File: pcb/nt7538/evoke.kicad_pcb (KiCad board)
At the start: 2 copper layers, 60 x 45 mm, 41 parts, among them J1 Conn_01x03_Male, J2 BACKLIGHT_CONN, Q1 Q_NMOS_GSD, U1 STM32F103C8Tx

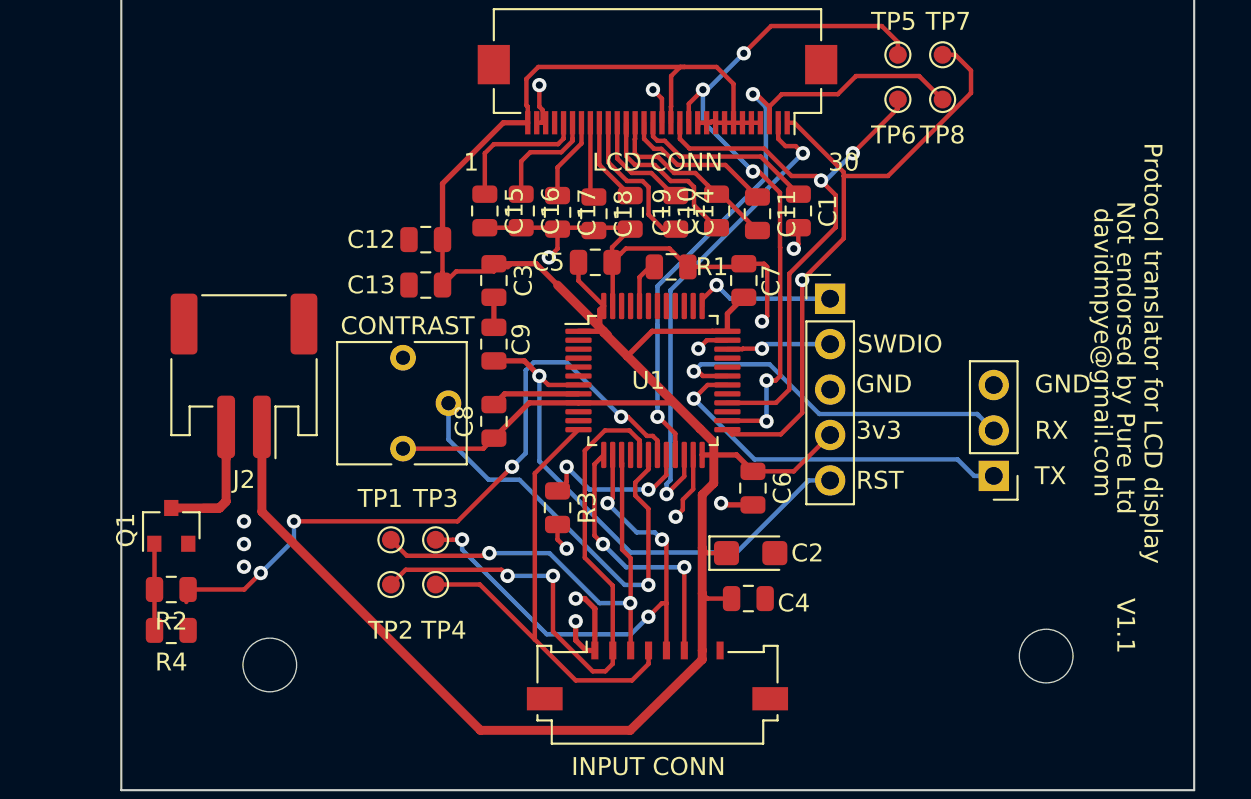
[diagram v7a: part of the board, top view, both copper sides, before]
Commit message: Updates to v1.2 for NT pcb - hole spacing redone
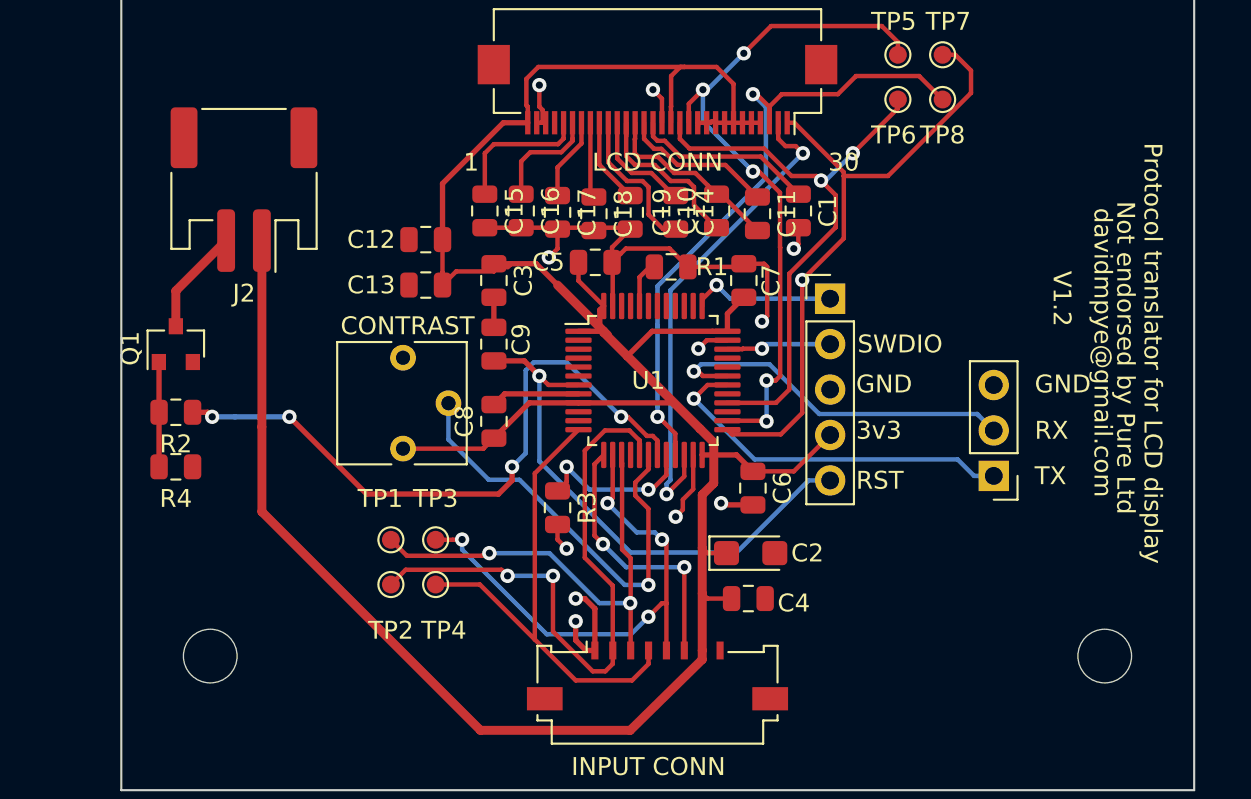
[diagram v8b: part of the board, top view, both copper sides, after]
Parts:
- moved J2 10.4 mm to (81.8, 42.9)
- moved Q1 10.2 mm to (78.0, 51.6)
- moved R2 9.91 mm to (78.0, 55.4)
- moved R4 9.15 mm to (78.0, 58.4)
- moved REF** 3.36 mm to (79.9, 69.0)
- moved REF** 3.27 mm to (129.9, 69.0)
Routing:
- net +3V3: track 151.0 -> 161.4 mm
- net Net-(J2-Pad2): track 8.83 -> 5.95 mm
- net LCD_BACKLIGHT_PWM: track 38.4 -> 36.7 mm
- net Net-(Q1-Pad1): track 4.85 -> 5.86 mm
- net GND: vias 14 -> 11
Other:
- board text added: "V1.2"
- board text removed: "V1.1"
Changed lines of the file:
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@@
     (thickness 1.6)
     (drawings 17)
-    (tracks 467)
+    (tracks 460)
     (zones 0)
     (modules 41)
@@
   )
   (setup
-    (last_trace_width 0.25)
+    (last_trace_width 0.3)
     (user_trace_width 0.3)
     (user_trace_width 0.5)
@@
   )
   (module MountingHole:MountingHole_3mm locked (layer F.Cu)
-    (at 126.63 69)
+    (at 129.902 69)
     (descr "Mounting Hole 3mm, no annular")
     (tags "mounting hole 3mm no annular")
@@
   )
   (module MountingHole:MountingHole_3mm locked (layer F.Cu)
-    (at 83.23 69.496)
+    (at 79.902 69)
     (descr "Mounting Hole 3mm, no annular")
     (tags "mounting hole 3mm no annular")
@@
   )
   (module Package_TO_SOT_SMD:SOT-23 (layer F.Cu)
-    (at 77.724 61.722 90)
+    (at 77.978 51.562 90)
     (descr "SOT-23, Standard")
     (tags SOT-23)
@@
   )
   (module Resistor_SMD:R_0805_2012Metric (layer F.Cu)
-    (at 77.724 65.278)
+    (at 77.978 55.372)
     (descr "Resistor SMD 0805 (2012 Metric), square (rectangular) end terminal, IPC_7351 nominal, (Body size source: https://docs.google.com/spreadsheets/d/1BsfQQcO9C6DZCsRaXUlFlo91Tg2WpOkGARC1WS5S8t0/edit?usp=sharing), generated with kicad-footprint-generator")
     (tags resistor)
@@
   )
   (module Resistor_SMD:R_0805_2012Metric (layer F.Cu)
-    (at 77.724 67.564)
+    (at 77.978 58.42)
     (descr "Resistor SMD 0805 (2012 Metric), square (rectangular) end terminal, IPC_7351 nominal, (Body size source: https://docs.google.com/spreadsheets/d/1BsfQQcO9C6DZCsRaXUlFlo91Tg2WpOkGARC1WS5S8t0/edit?usp=sharing), generated with kicad-footprint-generator")
     (tags resistor)
@@
   )
   (module Connector_JST:JST_PH_S2B-PH-SM4-TB_1x02-1MP_P2.00mm_Horizontal (layer F.Cu)
-    (at 81.788 53.34 180)
+    (at 81.788 42.926 180)
     (descr "JST PH series connector, S2B-PH-SM4-TB (http://www.jst-mfg.com/product/pdf/eng/ePH.pdf), generated with kicad-footprint-generator")
     (tags "connector JST PH top entry")
@@
     (effects (font (size 1 1) (thickness 0.2)))
   )
-  (gr_text V1.1 (at 131.064 67.31 270) (layer F.SilkS)
+  (gr_text V1.2 (at 127.508 49.022 270) (layer F.SilkS)
     (effects (font (size 1 1) (thickness 0.15)))
   )
@@
   (segment (start 95.007998 73.152) (end 103.378 73.152) (width 0.5) (layer F.Cu) (net 5))
   (segment (start 107.402 69.196002) (end 103.378 73.152) (width 0.5) (layer F.Cu) (net 5))
+  (segment (start 82.788 56.19) (end 82.788 45.776) (width 0.5) (layer F.Cu) (net 5))
   (segment (start 112.776 43.18) (end 110.67516 41.07916) (width 0.25) (layer F.Cu) (net 6))
   (segment (start 105.305582 40.195943) (end 104.896353 40.195943) (width 0.25) (layer F.Cu) (net 6))
@@
   (segment (start 105.57649 46.21899) (end 103.13301 46.21899) (width 0.25) (layer F.Cu) (net 35))
   (segment (start 106.6015 47.244) (end 105.57649 46.21899) (width 0.25) (layer F.Cu) (net 35))
-  (via (at 81.788 61.468) (size 0.8) (drill 0.4) (layers F.Cu B.Cu) (net 35))
-  (via (at 81.788 62.738) (size 0.8) (drill 0.4) (layers F.Cu B.Cu) (net 35))
-  (via (at 81.788 64.008) (size 0.8) (drill 0.4) (layers F.Cu B.Cu) (net 35))
   (via (at 98.298 37.084) (size 0.8) (drill 0.4) (layers F.Cu B.Cu) (net 35))
   (segment (start 98.298 38.292998) (end 98.298 37.084) (width 0.25) (layer F.Cu) (net 35))
@@
   (segment (start 101.652 41.5325) (end 101.652 39.188) (width 0.25) (layer F.Cu) (net 52))
   (segment (start 103.378 43.2585) (end 101.652 41.5325) (width 0.25) (layer F.Cu) (net 52))
-  (segment (start 76.7865 62.7345) (end 76.774 62.722) (width 0.25) (layer F.Cu) (net 53))
-  (segment (start 76.7865 67.564) (end 76.7865 62.7345) (width 0.25) (layer F.Cu) (net 53))
-  (segment (start 78.552 65.2655) (end 78.5645 65.278) (width 0.25) (layer F.Cu) (net 55))
-  (segment (start 78.5645 65.278) (end 78.5645 65.978) (width 0.25) (layer F.Cu) (net 55))
-  (segment (start 80.788 57.94) (end 80.788 56.19) (width 0.5) (layer F.Cu) (net 54))
-  (segment (start 80.788 60.352) (end 80.788 57.94) (width 0.5) (layer F.Cu) (net 54))
-  (segment (start 80.402 60.738) (end 80.788 60.352) (width 0.5) (layer F.Cu) (net 54))
-  (segment (start 79.502 60.738) (end 80.402 60.738) (width 0.5) (layer F.Cu) (net 54))
-  (segment (start 80.418 60.722) (end 80.788 60.352) (width 0.5) (layer F.Cu) (net 54))
-  (segment (start 77.724 60.722) (end 80.418 60.722) (width 0.5) (layer F.Cu) (net 54))
+  (segment (start 77.0405 58.42) (end 77.0405 55.372) (width 0.3) (layer F.Cu) (net 53))
+  (segment (start 77.0405 52.5745) (end 77.028 52.562) (width 0.3) (layer F.Cu) (net 53))
+  (segment (start 77.0405 55.372) (end 77.0405 52.5745) (width 0.3) (layer F.Cu) (net 53))
+  (segment (start 77.978 48.586) (end 80.788 45.776) (width 0.5) (layer F.Cu) (net 54))
+  (segment (start 77.978 50.562) (end 77.978 48.586) (width 0.5) (layer F.Cu) (net 54))
+  (segment (start 103.24141 55.626) (end 102.87 55.626) (width 0.25) (layer F.Cu) (net 55))
   (via (at 102.87 55.626) (size 0.8) (drill 0.4) (layers F.Cu B.Cu) (net 55))
-  (segment (start 103.24141 55.626) (end 102.87 55.626) (width 0.25) (layer F.Cu) (net 55))
+  (segment (start 104.898 56.953298) (end 104.638692 56.69399) (width 0.25) (layer F.Cu) (net 55))
+  (segment (start 104.638692 56.69399) (end 104.3094 56.69399) (width 0.25) (layer F.Cu) (net 55))
+  (segment (start 104.898 57.7565) (end 104.898 56.953298) (width 0.25) (layer F.Cu) (net 55))
+  (segment (start 97.536 57.658) (end 96.774 58.42) (width 0.25) (layer B.Cu) (net 55))
+  (via (at 96.774 58.42) (size 0.8) (drill 0.4) (layers F.Cu B.Cu) (net 55))
   (segment (start 104.3094 56.69399) (end 103.24141 55.626) (width 0.25) (layer F.Cu) (net 55))
-  (segment (start 104.638692 56.69399) (end 104.3094 56.69399) (width 0.25) (layer F.Cu) (net 55))
-  (segment (start 104.898 56.953298) (end 104.638692 56.69399) (width 0.25) (layer F.Cu) (net 55))
-  (segment (start 104.898 57.7565) (end 104.898 56.953298) (width 0.25) (layer F.Cu) (net 55))
+  (segment (start 97.536 53.028998) (end 97.536 57.658) (width 0.25) (layer B.Cu) (net 55))
+  (segment (start 99.822 52.578) (end 97.986998 52.578) (width 0.25) (layer B.Cu) (net 55))
+  (segment (start 97.986998 52.578) (end 97.536 53.028998) (width 0.25) (layer B.Cu) (net 55))
   (segment (start 102.87 55.626) (end 99.822 52.578) (width 0.25) (layer B.Cu) (net 55))
-  (segment (start 97.986998 52.578) (end 97.536 53.028998) (width 0.25) (layer B.Cu) (net 55))
-  (segment (start 99.822 52.578) (end 97.986998 52.578) (width 0.25) (layer B.Cu) (net 55))
-  (segment (start 97.536 53.028998) (end 97.536 57.658) (width 0.25) (layer B.Cu) (net 55))
-  (via (at 96.774 58.42) (size 0.8) (drill 0.4) (layers F.Cu B.Cu) (net 55))
-  (segment (start 97.536 57.658) (end 96.774 58.42) (width 0.25) (layer B.Cu) (net 55))
-  (via (at 84.582 61.468) (size 0.8) (drill 0.4) (layers F.Cu B.Cu) (net 55))
-  (via (at 82.72511 64.357039) (size 0.8) (drill 0.4) (layers F.Cu B.Cu) (net 55))
-  (segment (start 84.582 62.500149) (end 82.72511 64.357039) (width 0.25) (layer B.Cu) (net 55))
-  (segment (start 84.582 61.468) (end 84.582 62.500149) (width 0.25) (layer B.Cu) (net 55))
-  (segment (start 82.724072 64.356001) (end 82.513001 64.356001) (width 0.25) (layer F.Cu) (net 55))
-  (segment (start 82.72511 64.357039) (end 82.724072 64.356001) (width 0.25) (layer F.Cu) (net 55))
-  (segment (start 93.726 61.468) (end 96.774 58.42) (width 0.25) (layer F.Cu) (net 55))
-  (segment (start 84.582 61.468) (end 93.726 61.468) (width 0.25) (layer F.Cu) (net 55))
-  (segment (start 81.804149 65.278) (end 78.6615 65.278) (width 0.25) (layer F.Cu) (net 55))
-  (segment (start 82.72511 64.357039) (end 81.804149 65.278) (width 0.25) (layer F.Cu) (net 55))
+  (segment (start 96.774 58.42) (end 96.774 59.182) (width 0.3) (layer F.Cu) (net 55))
+  (segment (start 96.774 59.182) (end 96.012 59.944) (width 0.3) (layer F.Cu) (net 55))
+  (segment (start 96.012 59.944) (end 88.646 59.944) (width 0.3) (layer F.Cu) (net 55))
+  (via (at 84.328 55.626) (size 0.8) (drill 0.4) (layers F.Cu B.Cu) (net 55))
+  (segment (start 88.646 59.944) (end 84.328 55.626) (width 0.3) (layer F.Cu) (net 55))
+  (segment (start 84.328 55.626) (end 81.28 55.626) (width 0.3) (layer B.Cu) (net 55))
+  (via (at 80.01 55.626) (size 0.8) (drill 0.4) (layers F.Cu B.Cu) (net 55))
+  (segment (start 79.756 55.372) (end 80.01 55.626) (width 0.3) (layer F.Cu) (net 55))
+  (segment (start 78.9155 55.372) (end 79.756 55.372) (width 0.3) (layer F.Cu) (net 55))
+  (segment (start 81.28 55.626) (end 80.01 55.626) (width 0.3) (layer B.Cu) (net 55))
   (zone (net 35) (net_name GND) (layer B.Cu) (hatch edge 0.508)
     (connect_pads (clearance 0.508))
